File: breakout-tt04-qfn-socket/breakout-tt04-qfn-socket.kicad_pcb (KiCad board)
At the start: 2 copper layers, 45 x 52.5 mm, 101 parts, among them U1 Caravel_QFN_Socket

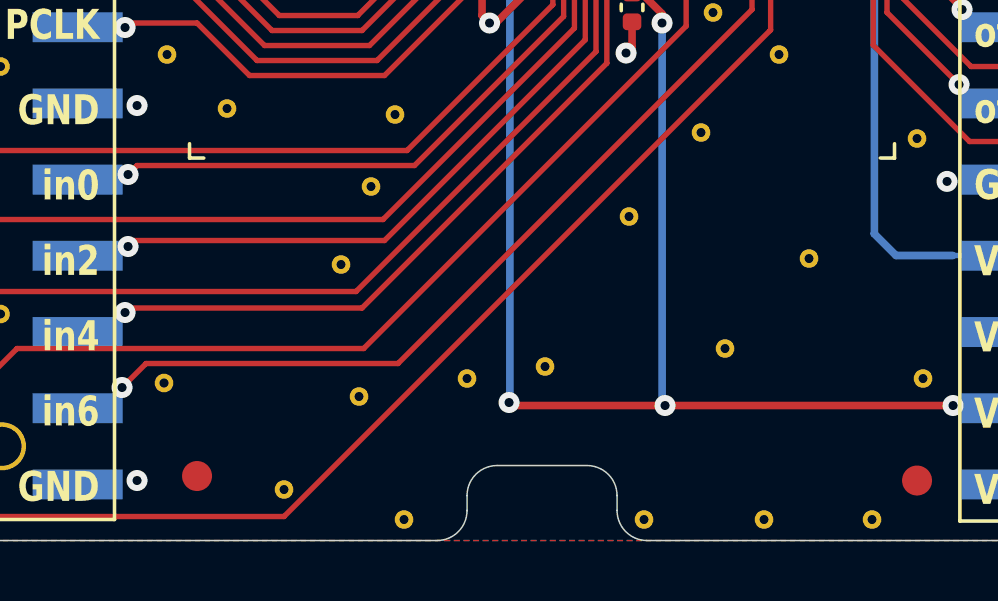
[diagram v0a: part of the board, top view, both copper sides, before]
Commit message: add logos
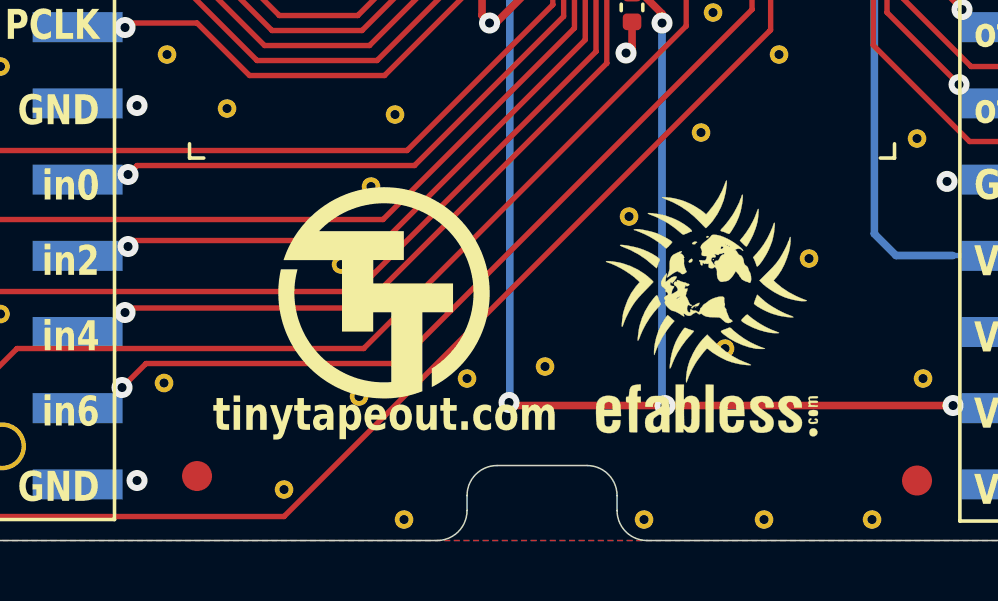
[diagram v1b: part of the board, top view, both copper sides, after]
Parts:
- added EFABLOG: Logo, Socket:ef_logo_graphical, F.Cu at (75.9, 61.4)
- added EFABTXT: Logo, Socket:ef_logo, F.Cu at (75.9, 65.7)
- added REF**: TT_logo, Socket:TT_logo, F.Cu at (65.3, 61.8)
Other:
- board text added: "tinytapeout.com"
